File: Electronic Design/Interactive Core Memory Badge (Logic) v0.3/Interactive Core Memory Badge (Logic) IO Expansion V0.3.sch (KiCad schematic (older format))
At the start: 22 parts

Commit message: Create PDF schematics
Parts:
- removed U? (x3): 74LS138, symbol 74xx_IEEE:74LS138
- added U7: SN74AUP1T34DCK, Package_TO_SOT_SMD:SOT-353_SC-70-5, symbol Logic_LevelTranslator:SN74AUP1T34DCK
- gave numbers to parts that had none: 7
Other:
- note added: "I2C ID: 0100xxx\nI2C address range is 32 decimal to 37 decimal or 0x20 to 0x27."
- note added: "I2C ID: ???????"
- note added: "TO DO: Board ID pin setting?\nIs there EEPROM setting in any of the I2C devices I’m using?"
- note added: "TO DO: I2C Address conflicts?"
- note added: "TO DO: Level shifter (74AHCT125 or 74HCT245) not required if using ~3.7V.\nor SN74LV1T34DCKR\nIs it fast enough?"
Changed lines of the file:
@@
 encoding utf-8
 Sheet 6 6
-Title ""
-Date ""
-Rev ""
+Title "Core 64 - IO Expansion"
+Date "2020-03-24"
+Rev "v0.3"
 Comp ""
 Comment1 ""
@@
 P 7500 1450
 AR Path="/5E755787/5EAA2FDC" Ref="U?"  Part="1"
-AR Path="/5EA63449/5EAA2FDC" Ref="U?"  Part="1"
-F 0 "U?" H 7500 1770 50  0000 C CNN
+AR Path="/5EA63449/5EAA2FDC" Ref="U8"  Part="1"
+F 0 "U8" H 7500 1770 50  0000 C CNN
 F 1 "74HC14" H 7500 1677 50  0000 C CNN
 F 2 "" H 7500 1450 50  0001 C CNN
@@
 P 7500 1950
 AR Path="/5E755787/5EAA2FE4" Ref="U?"  Part="2"
-AR Path="/5EA63449/5EAA2FE4" Ref="U?"  Part="2"
-F 0 "U?" H 7500 2270 50  0000 C CNN
+AR Path="/5EA63449/5EAA2FE4" Ref="U8"  Part="2"
+F 0 "U8" H 7500 2270 50  0000 C CNN
 F 1 "74HC14" H 7500 2177 50  0000 C CNN
 F 2 "" H 7500 1950 50  0001 C CNN
@@
 P 7500 2450
 AR Path="/5E755787/5EAA2FEA" Ref="U?"  Part="3"
-AR Path="/5EA63449/5EAA2FEA" Ref="U?"  Part="3"
-F 0 "U?" H 7500 2770 50  0000 C CNN
+AR Path="/5EA63449/5EAA2FEA" Ref="U8"  Part="3"
+F 0 "U8" H 7500 2770 50  0000 C CNN
 F 1 "74HC14" H 7500 2677 50  0000 C CNN
 F 2 "" H 7500 2450 50  0001 C CNN
@@
 P 7500 3000
 AR Path="/5E755787/5EAA2FF0" Ref="U?"  Part="4"
-AR Path="/5EA63449/5EAA2FF0" Ref="U?"  Part="4"
-F 0 "U?" H 7500 3320 50  0000 C CNN
+AR Path="/5EA63449/5EAA2FF0" Ref="U8"  Part="4"
+F 0 "U8" H 7500 3320 50  0000 C CNN
 F 1 "74HC14" H 7500 3227 50  0000 C CNN
 F 2 "" H 7500 3000 50  0001 C CNN
@@
 P 7500 3500
 AR Path="/5E755787/5EAA2FF6" Ref="U?"  Part="5"
-AR Path="/5EA63449/5EAA2FF6" Ref="U?"  Part="5"
-F 0 "U?" H 7500 3820 50  0000 C CNN
+AR Path="/5EA63449/5EAA2FF6" Ref="U8"  Part="5"
+F 0 "U8" H 7500 3820 50  0000 C CNN
 F 1 "74HC14" H 7500 3727 50  0000 C CNN
 F 2 "" H 7500 3500 50  0001 C CNN
@@
 P 7500 4050
 AR Path="/5E755787/5EAA2FFC" Ref="U?"  Part="6"
-AR Path="/5EA63449/5EAA2FFC" Ref="U?"  Part="6"
-F 0 "U?" H 7500 4370 50  0000 C CNN
+AR Path="/5EA63449/5EAA2FFC" Ref="U8"  Part="6"
+F 0 "U8" H 7500 4370 50  0000 C CNN
 F 1 "74HC14" H 7500 4277 50  0000 C CNN
 F 2 "" H 7500 4050 50  0001 C CNN
@@
 P 7550 4850
 AR Path="/5E755787/5EAA3002" Ref="U?"  Part="7"
-AR Path="/5EA63449/5EAA3002" Ref="U?"  Part="7"
-F 0 "U?" H 7780 4897 50  0000 L CNN
+AR Path="/5EA63449/5EAA3002" Ref="U8"  Part="7"
+F 0 "U8" H 7780 4897 50  0000 L CNN
 F 1 "74HC14" H 7780 4804 50  0000 L CNN
 F 2 "" H 7550 4850 50  0001 C CNN
@@
 P 9250 1450
 AR Path="/5E755787/5EAA3008" Ref="U?"  Part="1"
-AR Path="/5EA63449/5EAA3008" Ref="U?"  Part="1"
-F 0 "U?" H 9250 1770 50  0000 C CNN
+AR Path="/5EA63449/5EAA3008" Ref="U9"  Part="1"
+F 0 "U9" H 9250 1770 50  0000 C CNN
 F 1 "74HC14" H 9250 1677 50  0000 C CNN
 F 2 "" H 9250 1450 50  0001 C CNN
@@
 P 9250 1950
 AR Path="/5E755787/5EAA300E" Ref="U?"  Part="2"
-AR Path="/5EA63449/5EAA300E" Ref="U?"  Part="2"
-F 0 "U?" H 9250 2270 50  0000 C CNN
+AR Path="/5EA63449/5EAA300E" Ref="U9"  Part="2"
+F 0 "U9" H 9250 2270 50  0000 C CNN
 F 1 "74HC14" H 9250 2177 50  0000 C CNN
 F 2 "" H 9250 1950 50  0001 C CNN
@@
 P 9250 2450
 AR Path="/5E755787/5EAA3014" Ref="U?"  Part="3"
-AR Path="/5EA63449/5EAA3014" Ref="U?"  Part="3"
-F 0 "U?" H 9250 2770 50  0000 C CNN
+AR Path="/5EA63449/5EAA3014" Ref="U9"  Part="3"
+F 0 "U9" H 9250 2770 50  0000 C CNN
 F 1 "74HC14" H 9250 2677 50  0000 C CNN
 F 2 "" H 9250 2450 50  0001 C CNN
@@
 P 9250 3000
 AR Path="/5E755787/5EAA301A" Ref="U?"  Part="4"
-AR Path="/5EA63449/5EAA301A" Ref="U?"  Part="4"
-F 0 "U?" H 9250 3320 50  0000 C CNN
+AR Path="/5EA63449/5EAA301A" Ref="U9"  Part="4"
+F 0 "U9" H 9250 3320 50  0000 C CNN
 F 1 "74HC14" H 9250 3227 50  0000 C CNN
 F 2 "" H 9250 3000 50  0001 C CNN
@@
 P 9250 3550
 AR Path="/5E755787/5EAA3020" Ref="U?"  Part="5"
-AR Path="/5EA63449/5EAA3020" Ref="U?"  Part="5"
-F 0 "U?" H 9250 3870 50  0000 C CNN
+AR Path="/5EA63449/5EAA3020" Ref="U9"  Part="5"
+F 0 "U9" H 9250 3870 50  0000 C CNN
 F 1 "74HC14" H 9250 3777 50  0000 C CNN
 F 2 "" H 9250 3550 50  0001 C CNN
@@
 P 9250 4050
 AR Path="/5E755787/5EAA3026" Ref="U?"  Part="6"
-AR Path="/5EA63449/5EAA3026" Ref="U?"  Part="6"
-F 0 "U?" H 9250 4370 50  0000 C CNN
+AR Path="/5EA63449/5EAA3026" Ref="U9"  Part="6"
+F 0 "U9" H 9250 4370 50  0000 C CNN
 F 1 "74HC14" H 9250 4277 50  0000 C CNN
 F 2 "" H 9250 4050 50  0001 C CNN
@@
 P 9300 4850
 AR Path="/5E755787/5EAA302C" Ref="U?"  Part="7"
-AR Path="/5EA63449/5EAA302C" Ref="U?"  Part="7"
-F 0 "U?" H 9530 4897 50  0000 L CNN
+AR Path="/5EA63449/5EAA302C" Ref="U9"  Part="7"
+F 0 "U9" H 9530 4897 50  0000 L CNN
 F 1 "74HC14" H 9530 4804 50  0000 L CNN
 F 2 "" H 9300 4850 50  0001 C CNN
@@
 P 4100 2250
 AR Path="/5E755787/5EAA3044" Ref="U?"  Part="1"
-AR Path="/5EA63449/5EAA3044" Ref="U?"  Part="1"
-F 0 "U?" H 4100 3535 50  0000 C CNN
+AR Path="/5EA63449/5EAA3044" Ref="U5"  Part="1"
+F 0 "U5" H 4100 3535 50  0000 C CNN
 F 1 "MCP23017_SS" H 4100 3442 50  0000 C CNN
 F 2 "Package_SO:SSOP-28_5.3x10.2mm_P0.65mm" H 4300 1250 50  0001 L CNN
@@
 P 4100 4800
 AR Path="/5E755787/5EAA304A" Ref="U?"  Part="1"
-AR Path="/5EA63449/5EAA304A" Ref="U?"  Part="1"
-F 0 "U?" H 4100 6085 50  0000 C CNN
+AR Path="/5EA63449/5EAA304A" Ref="U6"  Part="1"
+F 0 "U6" H 4100 6085 50  0000 C CNN
 F 1 "MCP23017_SS" H 4100 5992 50  0000 C CNN
 F 2 "Package_SO:SSOP-28_5.3x10.2mm_P0.65mm" H 4300 3800 50  0001 L CNN
@@
 AR Path="/5E755787/5EAA93F9" Ref="H?"  Part="1"
 AR Path="/5E755AC8/5D2551FF/5EAA93F9" Ref="H?"  Part="1"
-AR Path="/5EA63449/5EAA93F9" Ref="H?"  Part="1"
-F 0 "H?" H 2008 7246 50  0000 L CNN
+AR Path="/5EA63449/5EAA93F9" Ref="H1"  Part="1"
+F 0 "H1" H 2008 7246 50  0000 L CNN
 F 1 "OLED_DISPLAY" H 2008 7155 50  0000 L CNN
 F 2 "Core_Memory_8x8_Array:OLED_Header_4PIN" H 1850 7160 50  0001 C CNN
@@
 AR Path="/5E755787/5EAA93FF" Ref="#PWR?"  Part="1"
 AR Path="/5E755AC8/5D2551FF/5EAA93FF" Ref="#PWR?"  Part="1"
-AR Path="/5EA63449/5EAA93FF" Ref="#PWR?"  Part="1"
-F 0 "#PWR?" H 1850 6700 50  0001 C CNN
+AR Path="/5EA63449/5EAA93FF" Ref="#PWR0123"  Part="1"
+F 0 "#PWR0123" H 1850 6700 50  0001 C CNN
 F 1 "+VSW" H 1865 7023 50  0000 C CNN
 F 2 "" H 1850 6850 50  0001 C CNN
@@
 AR Path="/5E755787/5EAA9409" Ref="C?"  Part="1"
 AR Path="/5E755AC8/5D2551FF/5EAA9409" Ref="C?"  Part="1"
-AR Path="/5EA63449/5EAA9409" Ref="C?"  Part="1"
-F 0 "C?" H 3291 7146 50  0000 L CNN
+AR Path="/5EA63449/5EAA9409" Ref="C2"  Part="1"
+F 0 "C2" H 3291 7146 50  0000 L CNN
 F 1 "10uF" H 3291 7055 50  0000 L CNN
 F 2 "Capacitor_SMD:C_0805_2012Metric" H 3200 7100 50  0001 C CNN
@@
 AR Path="/5E755787/5EAA940F" Ref="C?"  Part="1"
 AR Path="/5E755AC8/5D2551FF/5EAA940F" Ref="C?"  Part="1"
-AR Path="/5EA63449/5EAA940F" Ref="C?"  Part="1"
-F 0 "C?" H 2841 7146 50  0000 L CNN
+AR Path="/5EA63449/5EAA940F" Ref="C1"  Part="1"
+F 0 "C1" H 2841 7146 50  0000 L CNN
 F 1 "0.1uF" H 2841 7055 50  0000 L CNN
 F 2 "Capacitor_SMD:C_0805_2012Metric" H 2750 7100 50  0001 C CNN
@@
 P 1850 7400
 AR Path="/5E755787/5EAA9421" Ref="#PWR?"  Part="1"
-AR Path="/5EA63449/5EAA9421" Ref="#PWR?"  Part="1"
-F 0 "#PWR?" H 1850 7150 50  0001 C CNN
+AR Path="/5EA63449/5EAA9421" Ref="#PWR0124"  Part="1"
+F 0 "#PWR0124" H 1850 7150 50  0001 C CNN
 F 1 "GND" H 1855 7225 50  0000 C CNN
 F 2 "" H 1850 7400 50  0001 C CNN
@@
 	1850 7400 1850 7350
 Connection ~ 1850 7350
-$Comp
-L 74xx_IEEE:74LS138 U?
-U 1 1 5EAAB092
-P 1700 1600
-F 0 "U?" H 1700 2120 50  0000 C CNN
-F 1 "74LS138" H 1700 2027 50  0000 C CNN
-F 2 "" H 1700 1600 50  0001 C CNN
-F 3 "" H 1700 1600 50  0001 C CNN
-	1    1700 1600
-	1    0    0    -1
-$EndComp
-$Comp
-L 74xx_IEEE:74LS138 U?
-U 1 1 5EAACA96
-P 1700 2900
-F 0 "U?" H 1700 3420 50  0000 C CNN
-F 1 "74LS138" H 1700 3327 50  0000 C CNN
-F 2 "" H 1700 2900 50  0001 C CNN
-F 3 "" H 1700 2900 50  0001 C CNN
-	1    1700 2900
-	1    0    0    -1
-$EndComp
-$Comp
-L 74xx_IEEE:74LS138 U?
-U 1 1 5EAAEE78
-P 1700 4250
-F 0 "U?" H 1700 4770 50  0000 C CNN
-F 1 "74LS138" H 1700 4677 50  0000 C CNN
-F 2 "" H 1700 4250 50  0001 C CNN
-F 3 "" H 1700 4250 50  0001 C CNN
-	1    1700 4250
-	1    0    0    -1
-$EndComp
+Text Notes 4900 5850 0    50   ~ 10
+TO DO: Board ID pin setting?\nIs there EEPROM setting in any of the I2C devices I’m using?
+Text Notes 1150 3550 0    50   ~ 0
+I2C ID: 0100xxx\nI2C address range is 32 decimal to 37 decimal or 0x20 to 0x27.
+Text Notes 2250 6700 0    50   ~ 0
+I2C ID: ???????
+Text Notes 3950 6850 0    50   ~ 10
+TO DO: Level shifter (74AHCT125 or 74HCT245) not required if using ~3.7V.\nor SN74LV1T34DCKR\nIs it fast enough?
+$Comp
+L Logic_LevelTranslator:SN74AUP1T34DCK U7
+U 1 1 5E7BAA1F
+P 4200 7300
+F 0 "U7" H 4645 7347 50  0000 L CNN
+F 1 "SN74AUP1T34DCK" H 4645 7254 50  0000 L CNN
+F 2 "Package_TO_SOT_SMD:SOT-353_SC-70-5" H 4200 6600 50  0001 C CNN
+F 3 "http://www.ti.com/lit/ds/symlink/sn74aup1t34.pdf" H 4200 6700 50  0001 C CNN
+	1    4200 7300
+	1    0    0    -1
+$EndComp
+Text Notes 1100 1050 0    50   ~ 10
+TO DO: I2C Address conflicts?
 $EndSCHEMATC

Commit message: Schematic refinement
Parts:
- removed H1: OLED_DISPLAY, Core_Memory_8x8_Array:OLED_Header_4PIN, symbol Motor:Fan_4pin
- removed U5, U6: MCP23017_SS, Package_SO:SSOP-28_5.3x10.2mm_P0.65mm, symbol Interface_Expansion:MCP23017_SS
- removed U7: SN74AUP1T34DCK, Package_TO_SOT_SMD:SOT-353_SC-70-5, symbol Logic_LevelTranslator:SN74AUP1T34DCK
- added J5: Conn_01x04_Female, Connector_PinSocket_2.54mm:PinSocket_1x04_P2.54mm_Vertical_SMD_and_TH_Pin1Left, symbol Connector:Conn_01x04_Female
- added R47, R48, R49, R50, R6, R7: 10K, Resistor_SMD:R_0805_2012Metric, symbol Device:R
- added U5, U6: MCP23017_SO, Package_SO:SOIC-28W_7.5x17.9mm_P1.27mm, symbol Interface_Expansion:MCP23017_SO
- added X1, X2, X3: SAO_v169bis, badgelife_sao_v169bis:Badgelife-SAOv169-BADGE-2x3, symbol badgelife_shitty_addon_v169bis:Badgelife_sao_connector_v169bis
- U8, U9: footprint (none) -> Digikey:SOIC-14_W3.9mm
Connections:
- net labels added: 3V3_100mA, 3V3_800mA, BOARD_ID1, BOARD_ID2, BOARD_ID3, GNDD, SAO1_GPIO1(TX), SAO1_GPIO2(RX), SAO2_GPIO1(TX), SAO2_GPIO2(RX), SAO3_GPIO1, SAO3_GPIO2
- wire segments 11 -> 73
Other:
- note added: "0.96” (128x64)\nI2C 4-pins, ADDRESS: 0x3C\n(alternate is 0x3D, not 0x7A or 0x78!)"
- note added: "0b001 = 0x01 = 1\nTop 3 resistors: DNI, DNI, 10K\nBottom 3 resistors: 10K, 10K, DNI"
- note added: "A.K.A. SAO v1.69bis using Sullins SFH11-NBPC-D03-ST-BK\nhttps://www.digikey.com/product-detail/en/sullins-connector-solutions/SFH11-NBPC-D03-ST-BK/S9717-ND/4558818"
- note added: "BOARD ID"
- note added: "OLED DISPLAY (OPTIONAL)"
- note added: "SUPERIOR ADD-ON SOCKET (OPTIONAL)"
- note removed: "I2C ID: ???????"
- note removed: "TO DO: Board ID pin setting?\nIs there EEPROM setting in any of the I2C devices I’m using?"
- note removed: "TO DO: Level shifter (74AHCT125 or 74HCT245) not required if using ~3.7V.\nor SN74LV1T34DCKR\nIs it fast enough?"
- note removed: "TO DO: Update this to be SAO, and some easy to add I2C OLED 4-pin header."
- moved on the sheet: C1, C2, U8G, U9G

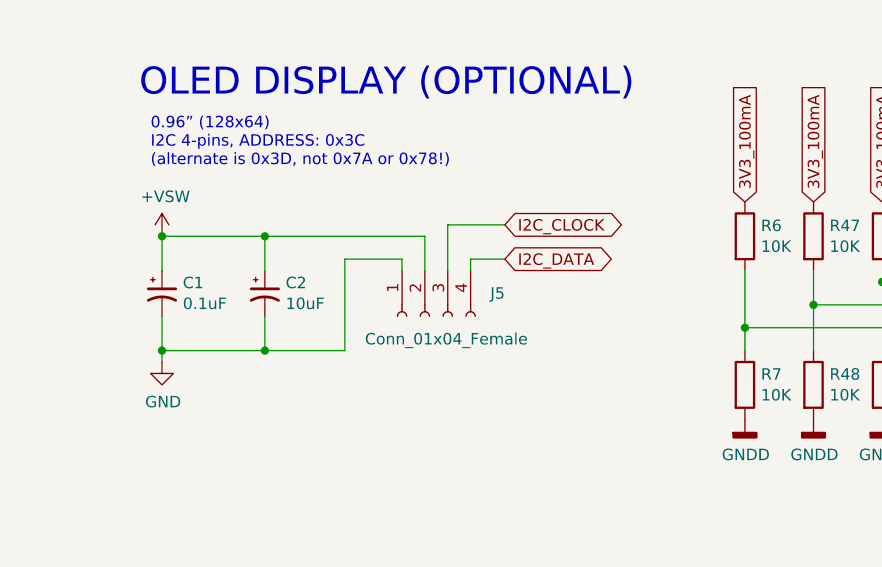
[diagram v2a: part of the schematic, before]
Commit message: Added OLED power solder jumpers
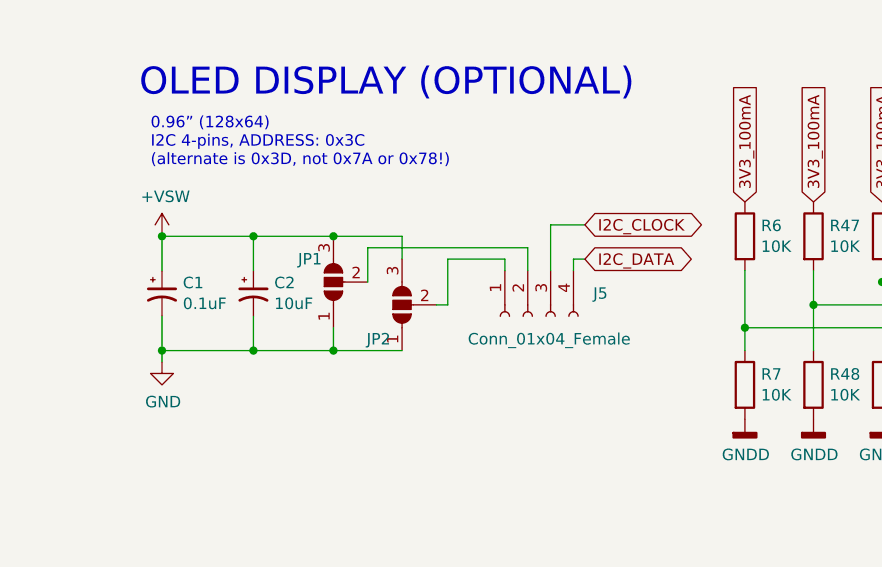
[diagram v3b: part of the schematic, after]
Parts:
- added JP1, JP2: SolderJumper_3_Open, Jumper:SolderJumper-3_P1.3mm_Open_Pad1.0x1.5mm_NumberLabels, symbol Jumper:SolderJumper_3_Open
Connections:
- net +VSW: now also JP1.3 (B), JP2.3 (B); no longer J5.2 (Pin_2)
- net GND: now also JP1.1 (A), JP2.1 (A); no longer J5.1 (Pin_1)
- new net: J5.1 (Pin_1), JP2.2 (C)
- new net: J5.2 (Pin_2), JP1.2 (C)
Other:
- moved on the sheet: C2, J5
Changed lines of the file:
@@
 	1    0    0    -1
 $EndComp
-Text GLabel 7850 5400 2    50   BiDi ~ 0
+Text GLabel 8200 5400 2    50   BiDi ~ 0
 I2C_CLOCK
-Text GLabel 7850 5550 2    50   BiDi ~ 0
+Text GLabel 8200 5550 2    50   BiDi ~ 0
 I2C_DATA
 Wire Wire Line
-	7850 5550 7700 5550
+	8200 5550 8150 5550
 $Comp
 L Device:CP1_Small C?
 U 1 1 5EAA9409
-P 6800 5700
+P 6750 5700
 AR Path="/5E755787/5EAA9409" Ref="C?"  Part="1"
 AR Path="/5E755AC8/5D2551FF/5EAA9409" Ref="C?"  Part="1"
 AR Path="/5EA63449/5EAA9409" Ref="C2"  Part="1"
-F 0 "C2" H 6891 5746 50  0000 L CNN
-F 1 "10uF" H 6891 5655 50  0000 L CNN
-F 2 "Capacitor_SMD:C_0805_2012Metric" H 6800 5700 50  0001 C CNN
-F 3 "~" H 6800 5700 50  0001 C CNN
-	1    6800 5700
+F 0 "C2" H 6841 5746 50  0000 L CNN
+F 1 "10uF" H 6841 5655 50  0000 L CNN
+F 2 "Capacitor_SMD:C_0805_2012Metric" H 6750 5700 50  0001 C CNN
+F 3 "~" H 6750 5700 50  0001 C CNN
+	1    6750 5700
 	1    0    0    -1
 $EndComp
@@
 $EndComp
 Wire Wire Line
-	6800 5450 6800 5600
-Wire Wire Line
-	6800 5800 6800 5950
-Wire Wire Line
-	6800 5950 6350 5950
+	6750 5450 6750 5600
+Wire Wire Line
+	6750 5800 6750 5950
 Wire Wire Line
 	6350 5600 6350 5450
 Connection ~ 6350 5450
 Wire Wire Line
-	6350 5450 6800 5450
+	6350 5450 6750 5450
 Wire Wire Line
 	6350 5800 6350 5950
@@
 L Connector:Conn_01x04_Female J5
 U 1 1 5E830BC9
-P 7500 5800
-F 0 "J5" V 7400 5450 50  0000 L CNN
-F 1 "Conn_01x04_Female" V 7600 5350 50  0000 L CNN
-F 2 "Connector_PinSocket_2.54mm:PinSocket_1x04_P2.54mm_Vertical_SMD_and_TH_Pin1Left" H 7500 5800 50  0001 C CNN
-F 3 "~" H 7500 5800 50  0001 C CNN
-	1    7500 5800
+P 7950 5800
+F 0 "J5" V 7850 5450 50  0000 L CNN
+F 1 "Conn_01x04_Female" V 8050 5350 50  0000 L CNN
+F 2 "Connector_PinSocket_2.54mm:PinSocket_1x04_P2.54mm_Vertical_SMD_and_TH_Pin1Left" H 7950 5800 50  0001 C CNN
+F 3 "~" H 7950 5800 50  0001 C CNN
+	1    7950 5800
 	0    -1   1    0
 $EndComp
 Wire Wire Line
-	7700 5600 7700 5550
-Wire Wire Line
-	7600 5400 7600 5600
-Wire Wire Line
-	7600 5400 7850 5400
-Wire Wire Line
-	6800 5450 7500 5450
-Wire Wire Line
-	7500 5450 7500 5600
-Connection ~ 6800 5450
-Wire Wire Line
-	6800 5950 7150 5950
-Wire Wire Line
-	7150 5950 7150 5550
-Wire Wire Line
-	7150 5550 7400 5550
-Connection ~ 6800 5950
-Wire Wire Line
-	7400 5550 7400 5600
+	8150 5600 8150 5550
+Wire Wire Line
+	8050 5400 8050 5600
+Wire Wire Line
+	8050 5400 8200 5400
+Wire Wire Line
+	7250 5500 7950 5500
+Wire Wire Line
+	7950 5500 7950 5600
+Connection ~ 6750 5950
+Wire Wire Line
+	7850 5550 7850 5600
 Text Notes 6300 5150 0    50   ~ 0
 0.96” (128x64)\nI2C 4-pins, ADDRESS: 0x3C\n(alternate is 0x3D, not 0x7A or 0x78!)
@@
 Wire Wire Line
 	4950 7200 5000 7200
+$Comp
+L Jumper:SolderJumper_3_Open JP2
+U 1 1 5E81A96A
+P 7400 5750
+F 0 "JP2" V 7250 5800 50  0000 L CNN
+F 1 "SolderJumper_3_Open" V 7000 5300 50  0001 L CNN
+F 2 "Jumper:SolderJumper-3_P1.3mm_Open_Pad1.0x1.5mm_NumberLabels" H 7400 5750 50  0001 C CNN
+F 3 "~" H 7400 5750 50  0001 C CNN
+	1    7400 5750
+	0    -1   -1   0
+$EndComp
+$Comp
+L Jumper:SolderJumper_3_Open JP1
+U 1 1 5E82F3CE
+P 7100 5650
+F 0 "JP1" V 7200 5700 50  0000 L CNN
+F 1 "SolderJumper_3_Open" V 6450 5550 50  0001 L CNN
+F 2 "Jumper:SolderJumper-3_P1.3mm_Open_Pad1.0x1.5mm_NumberLabels" H 7100 5650 50  0001 C CNN
+F 3 "~" H 7100 5650 50  0001 C CNN
+	1    7100 5650
+	0    -1   -1   0
+$EndComp
+Wire Wire Line
+	7600 5550 7850 5550
+Wire Wire Line
+	7550 5750 7600 5750
+Wire Wire Line
+	7600 5750 7600 5550
+Wire Wire Line
+	7250 5650 7250 5500
+Wire Wire Line
+	7100 5950 7100 5850
+Connection ~ 7100 5950
+Wire Wire Line
+	7100 5950 7400 5950
+Wire Wire Line
+	7100 5450 7400 5450
+Wire Wire Line
+	7400 5450 7400 5550
+Wire Wire Line
+	6750 5950 6350 5950
+Wire Wire Line
+	6750 5950 7100 5950
+Wire Wire Line
+	6750 5450 7100 5450
+Connection ~ 6750 5450
+Connection ~ 7100 5450
 $EndSCHEMATC
